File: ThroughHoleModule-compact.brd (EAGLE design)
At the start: 49.5 x 49.5 mm, 14 parts, among them IC1 K155ID1, IC2 K155ID1

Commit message: manufacture-ready
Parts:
- added U$1: (no value), SparkFun:OSHW-LOGO-S
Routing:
- net 2D: track 38.3 -> 39.3 mm
- net 2C: track 36.5 -> 37.1 mm
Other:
- board text added: "REV A"
- board text added: "http://git.io/kpS-Pw"

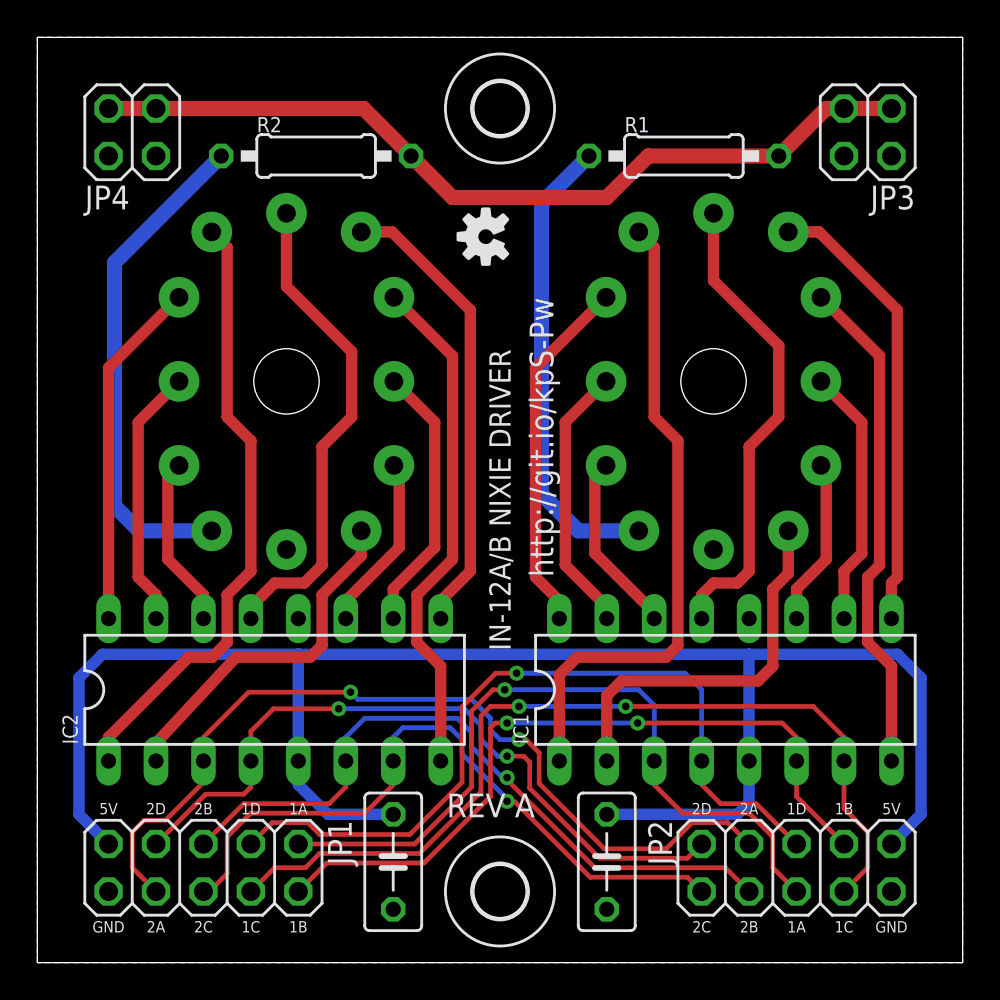
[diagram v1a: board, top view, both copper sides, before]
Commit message: Enlarged IN-12 mounting holes
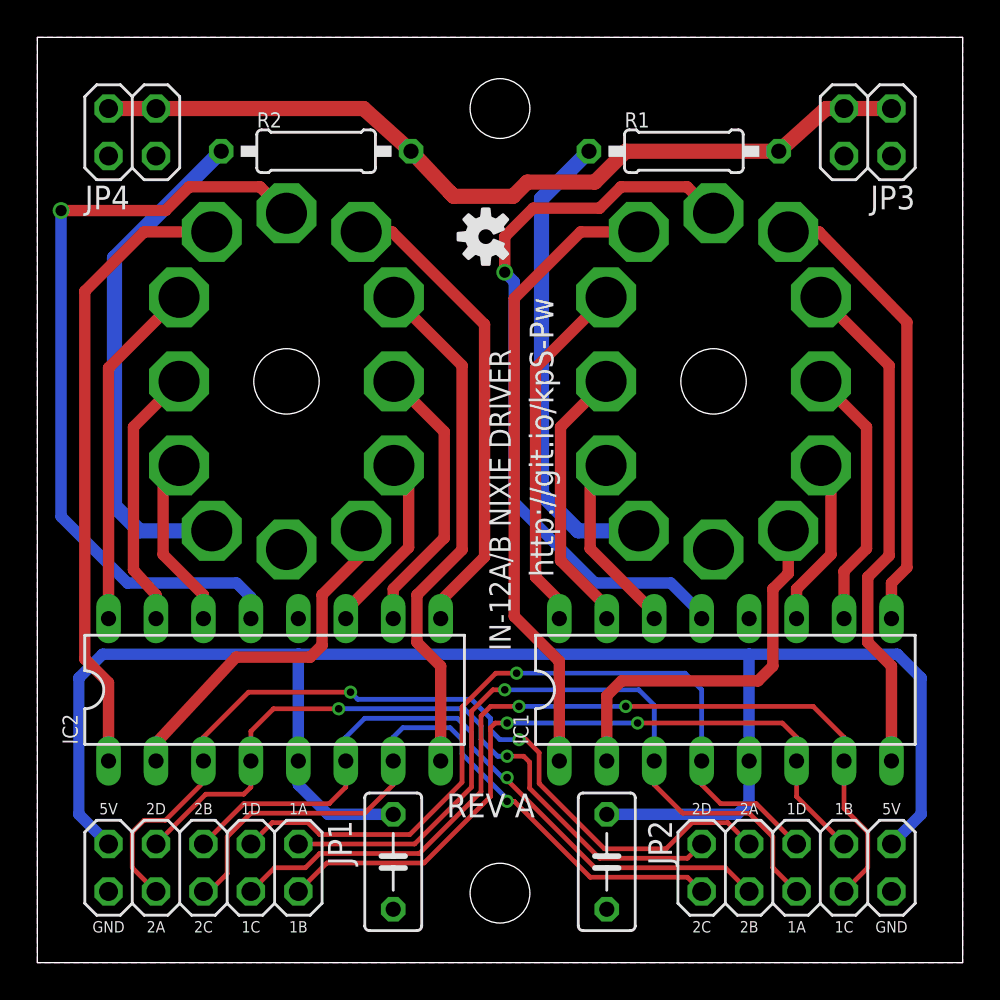
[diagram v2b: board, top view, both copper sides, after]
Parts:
- removed H1, H2: MOUNT-HOLE2.8, holes:2,8
- N1, N2: device mylib:IN-12 -> ThroughHoleModule-compact:IN-12
- moved R1 0.25 mm to (34.6, 43.4)
- moved R2 0.25 mm to (14.9, 43.4)
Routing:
- net N$2: track 26.3 -> 42.7 mm, vias 0 -> 1
- net N$4: track 25.6 -> 40.3 mm, vias 0 -> 1
- net N$3: track 34.6 -> 33.9 mm
- net N$1: track 33.1 -> 33.8 mm
- net N$9: track 24.7 -> 25.4 mm

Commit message: Reduced size for panelisation
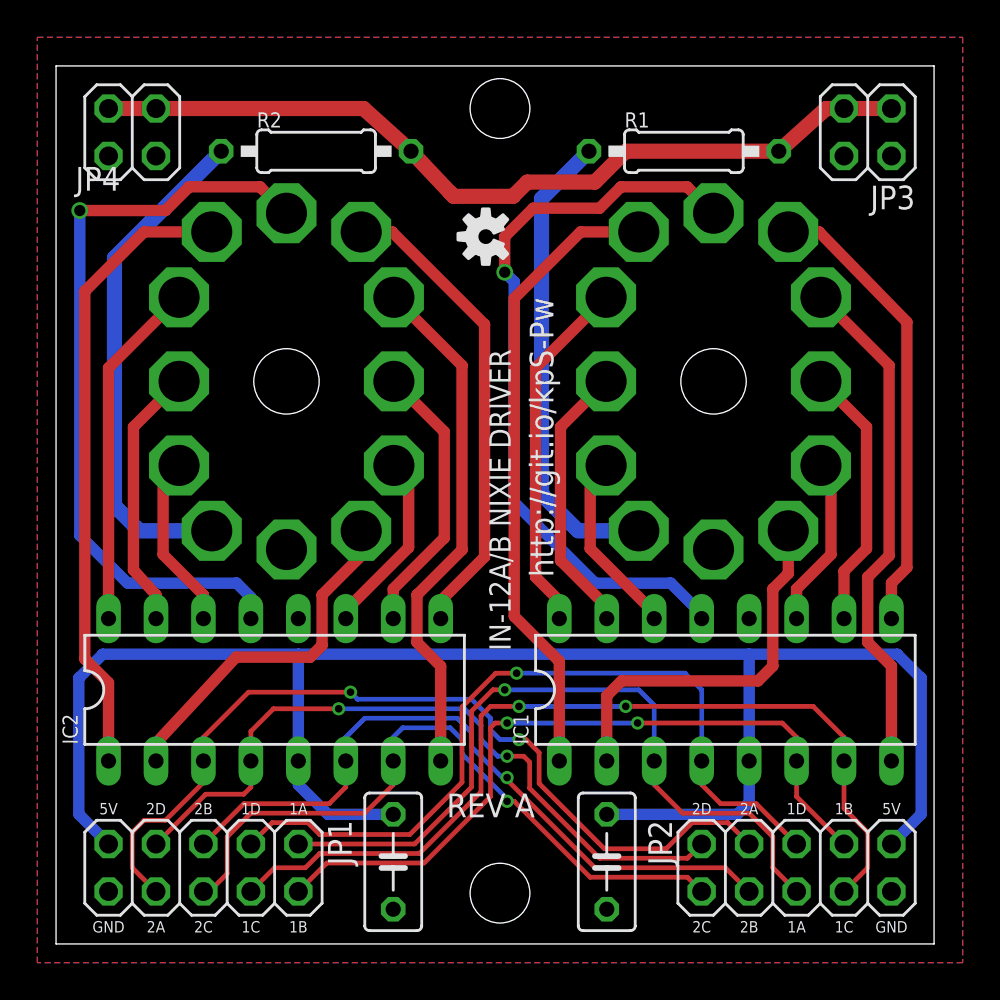
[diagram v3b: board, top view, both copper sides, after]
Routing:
- net N$2: track 42.7 -> 41.2 mm
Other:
- board size 49.5 x 49.5 mm -> 47 x 47 mm
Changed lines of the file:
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@@
 <setting verticaltext="up"/>
 </settings>
-<grid distance="1" unitdist="mm" unit="mm" style="lines" multiple="1" display="yes" altdistance="12.5" altunitdist="mil" altunit="mil"/>
+<grid distance="0.5" unitdist="mm" unit="mm" style="lines" multiple="1" display="yes" altdistance="12.5" altunitdist="mil" altunit="mil"/>
 <layers>
 <layer number="1" name="Top" color="4" fill="1" visible="yes" active="yes"/>
@@
 <board>
 <plain>
-<wire x1="0" y1="0" x2="49.53" y2="0" width="0" layer="20"/>
-<wire x1="49.53" y1="0" x2="49.53" y2="49.53" width="0" layer="20"/>
-<wire x1="49.53" y1="49.53" x2="0" y2="49.53" width="0" layer="20"/>
-<wire x1="0" y1="49.53" x2="0" y2="0" width="0" layer="20"/>
+<wire x1="1" y1="1" x2="48" y2="1" width="0" layer="20"/>
+<wire x1="48" y1="1" x2="48" y2="48" width="0" layer="20"/>
+<wire x1="48" y1="48" x2="1" y2="48" width="0" layer="20"/>
+<wire x1="1" y1="48" x2="1" y2="1" width="0" layer="20"/>
 <text x="24.765" y="24.765" size="1.143" layer="25" ratio="10" rot="R90" align="center">IN-12A/B NIXIE DRIVER</text>
 <text x="11.43" y="7.9375" size="0.6096" layer="21" align="bottom-center">1D</text>
@@
 </element>
 <element name="JP4" library="pinhead" package="2X02" value="" x="5.08" y="44.45" smashed="yes">
-<attribute name="NAME" x="2.54" y="40.3225" size="1.27" layer="25" ratio="10"/>
+<attribute name="NAME" x="2.04" y="41.3225" size="1.27" layer="25" ratio="10"/>
 <attribute name="VALUE" x="2.54" y="40.005" size="1.27" layer="27"/>
 </element>
@@
 <wire x1="11.43" y1="19.558" x2="10.668" y2="20.32" width="0.6096" layer="16"/>
 <wire x1="10.668" y1="20.32" x2="4.826" y2="20.32" width="0.6096" layer="16"/>
-<wire x1="4.826" y1="20.32" x2="1.27" y2="23.876" width="0.6096" layer="16"/>
-<wire x1="1.27" y1="23.876" x2="1.27" y2="40.259" width="0.6096" layer="16"/>
-<via x="1.27" y="40.259" extent="1-16" drill="0.6" shape="octagon"/>
-<wire x1="1.27" y1="40.259" x2="6.858" y2="40.259" width="0.6096" layer="1"/>
+<wire x1="4.826" y1="20.32" x2="2.27" y2="22.876" width="0.6096" layer="16"/>
+<wire x1="2.27" y1="22.876" x2="2.27" y2="40.259" width="0.6096" layer="16"/>
+<via x="2.27" y="40.259" extent="1-16" drill="0.6" shape="octagon"/>
+<wire x1="2.27" y1="40.259" x2="6.858" y2="40.259" width="0.6096" layer="1"/>
 <wire x1="6.858" y1="40.259" x2="8.128" y2="41.529" width="0.6096" layer="1"/>
 <wire x1="8.128" y1="41.529" x2="11.921" y2="41.529" width="0.6096" layer="1"/>
